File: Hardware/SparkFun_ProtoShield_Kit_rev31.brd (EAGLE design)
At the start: 53.3 x 68.6 mm, 29 parts

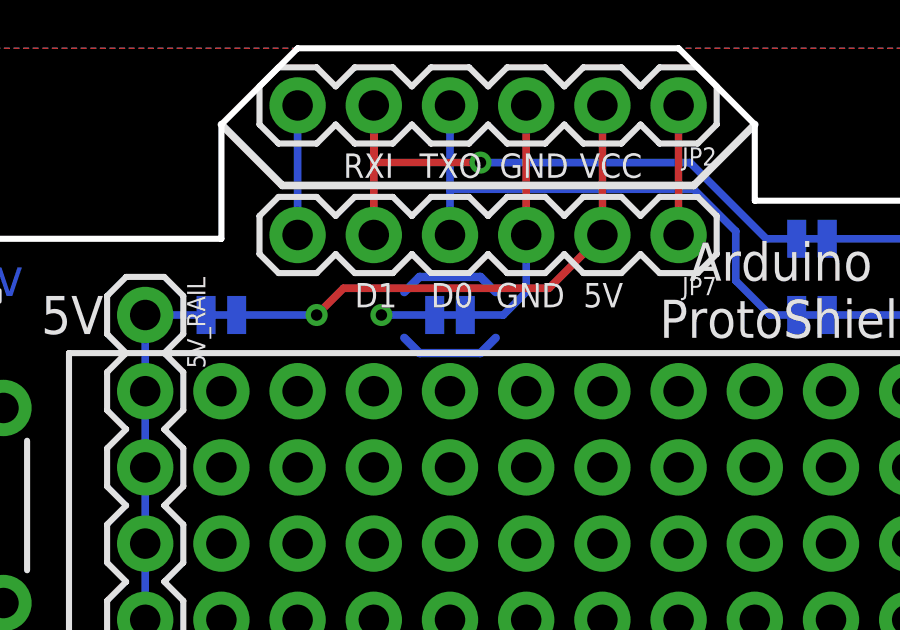
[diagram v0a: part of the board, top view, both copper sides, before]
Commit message: Add files via upload
**Board**

* Change wire boundary to bRestrict layer to prevent ground pour from creating a thermal around GND jumper pads.

**Schematic**

* Move OSHW logo next to SparkFun logo
* Move schematic components around to make use of the empty space
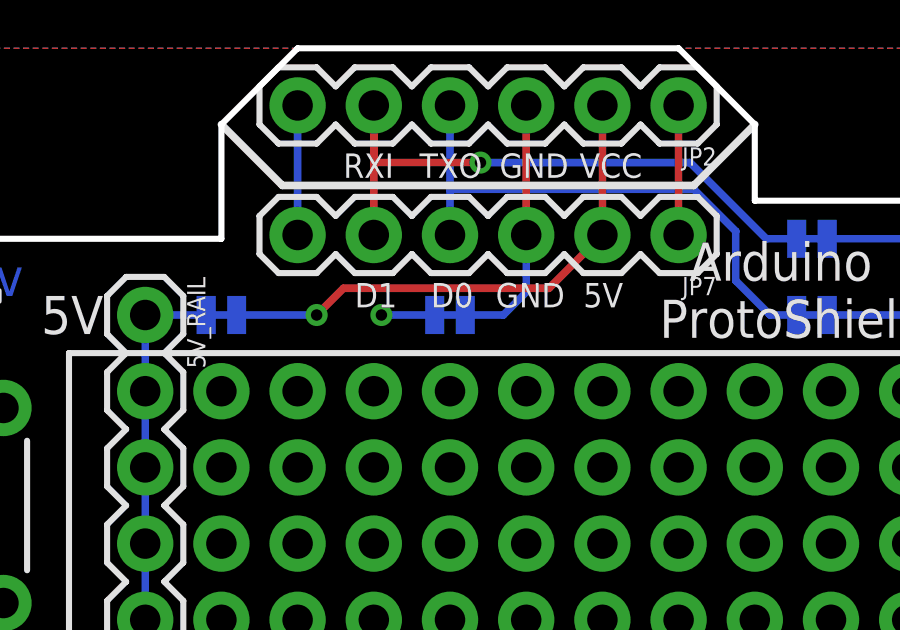
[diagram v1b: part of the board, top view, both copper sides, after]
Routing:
- net N$2: track 3.47 -> 0.00 mm
- net N$9: track 3.47 -> 0.00 mm
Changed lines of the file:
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@@
 <layer number="39" name="tKeepout" color="4" fill="11" visible="no" active="yes"/>
 <layer number="40" name="bKeepout" color="1" fill="11" visible="no" active="yes"/>
-<layer number="41" name="tRestrict" color="4" fill="10" visible="no" active="yes"/>
-<layer number="42" name="bRestrict" color="1" fill="10" visible="no" active="yes"/>
+<layer number="41" name="tRestrict" color="4" fill="10" visible="yes" active="yes"/>
+<layer number="42" name="bRestrict" color="1" fill="10" visible="yes" active="yes"/>
 <layer number="43" name="vRestrict" color="2" fill="10" visible="no" active="yes"/>
 <layer number="44" name="Drills" color="7" fill="1" visible="yes" active="yes"/>
@@
 <wire x1="24.765" y1="12.7" x2="24.13" y2="12.065" width="0.254" layer="22"/>
 <wire x1="29.7942" y1="13.0302" x2="31.0642" y2="13.0302" width="0.2032" layer="22"/>
+<wire x1="20.574" y1="60.198" x2="20.574" y2="60.579" width="0.254" layer="42"/>
+<wire x1="20.574" y1="60.579" x2="22.606" y2="60.579" width="0.254" layer="42"/>
+<wire x1="22.606" y1="60.579" x2="22.606" y2="60.198" width="0.254" layer="42"/>
+<wire x1="22.606" y1="59.309" x2="22.606" y2="58.801" width="0.254" layer="42"/>
+<wire x1="22.606" y1="58.801" x2="20.574" y2="58.801" width="0.254" layer="42"/>
+<wire x1="20.574" y1="58.801" x2="20.574" y2="59.309" width="0.254" layer="42"/>
 </plain>
 <attributes>
@@
 <wire x1="18.034" y1="60.579" x2="17.145" y2="59.69" width="0.254" layer="1"/>
 </signal>
-<signal name="N$2">
-<wire x1="23.114" y1="60.452" x2="22.606" y2="60.96" width="0.2794" layer="16"/>
-<wire x1="22.606" y1="60.96" x2="20.574" y2="60.96" width="0.2794" layer="16"/>
-<wire x1="20.574" y1="60.96" x2="20.066" y2="60.452" width="0.2794" layer="16"/>
-</signal>
-<signal name="N$9">
-<wire x1="20.066" y1="58.928" x2="20.574" y2="58.42" width="0.2794" layer="16"/>
-<wire x1="20.574" y1="58.42" x2="22.606" y2="58.42" width="0.2794" layer="16"/>
-<wire x1="22.606" y1="58.42" x2="23.114" y2="58.928" width="0.2794" layer="16"/>
-</signal>
 <signal name="A0">
